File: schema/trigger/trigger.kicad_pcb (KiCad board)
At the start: 2 copper layers, 12 parts, among them J1 Barrel_Jack, Q1 DMG4800LK3-13

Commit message: some new packages
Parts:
- removed C5: 10mF/25V, Capacitor_THT:CP_Radial_D18.0mm_P7.50mm
- added C7: 10n, Capacitor_SMD:C_0603_1608Metric, F.Cu at (187.1, 19.3)
- added C8: 100n, Capacitor_SMD:C_0603_1608Metric, F.Cu at (187.1, 21.8)
- added D2: LED_Small, LED_SMD:LED_0805_2012Metric, F.Cu at (160.9, 49.1)
- added IC2: SSD1306, myLibrary:OLED_I2C_128x64_THT, F.Cu at (171.9, 21.1)
- added R10: 1k0, Resistor_SMD:R_0603_1608Metric, F.Cu at (187.1, 39.4)
- added R4: 860k, Resistor_SMD:R_0603_1608Metric, F.Cu at (187.1, 24.3)
- added R5: 100k, Resistor_SMD:R_0603_1608Metric, F.Cu at (187.1, 26.8)
- added R6: 1k0, Resistor_SMD:R_0603_1608Metric, F.Cu at (187.1, 29.3)
- added R7: 4k7, Resistor_SMD:R_0603_1608Metric, F.Cu at (187.1, 31.8)
- added R8: 4k7, Resistor_SMD:R_0603_1608Metric, F.Cu at (187.1, 34.4)
- added R9: 1k0, Resistor_SMD:R_0603_1608Metric, F.Cu at (187.1, 36.9)
- C1, C2, C3, C4: footprint Capacitor_THT:CP_Radial_D18.0mm_P7.50mm -> myLibrary:C_36x18; moved to B.Cu
- D1: value SS28 -> LED_Small; footprint Diode_SMD:D_SMB -> LED_SMD:LED_0805_2012Metric
- moved C1 90.6 mm to (71.1, 128.3), turned to 180 degrees
- moved C2 65.6 mm to (91.4, 128.3), turned to 180 degrees
- moved C3 44.5 mm to (111.8, 128.3), turned to 180 degrees
- moved C4 35.3 mm to (132.1, 128.3), turned to 180 degrees
- moved D1 34.8 mm to (160.9, 46.1)
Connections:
- D1 pad 1: VCC -> GND
- J1 pad 1: Net-(D1-A) -> VCC

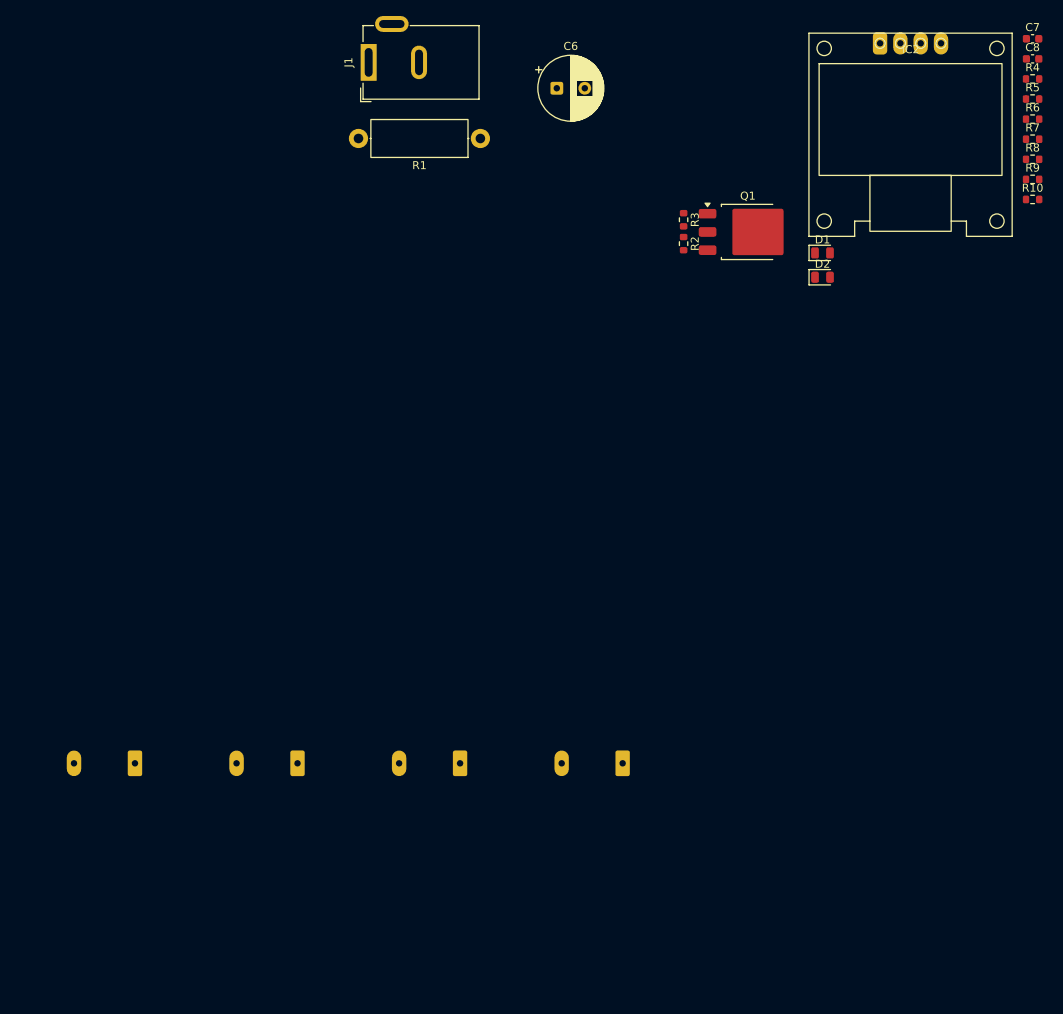
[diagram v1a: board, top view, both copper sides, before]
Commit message: yet another oled footprint
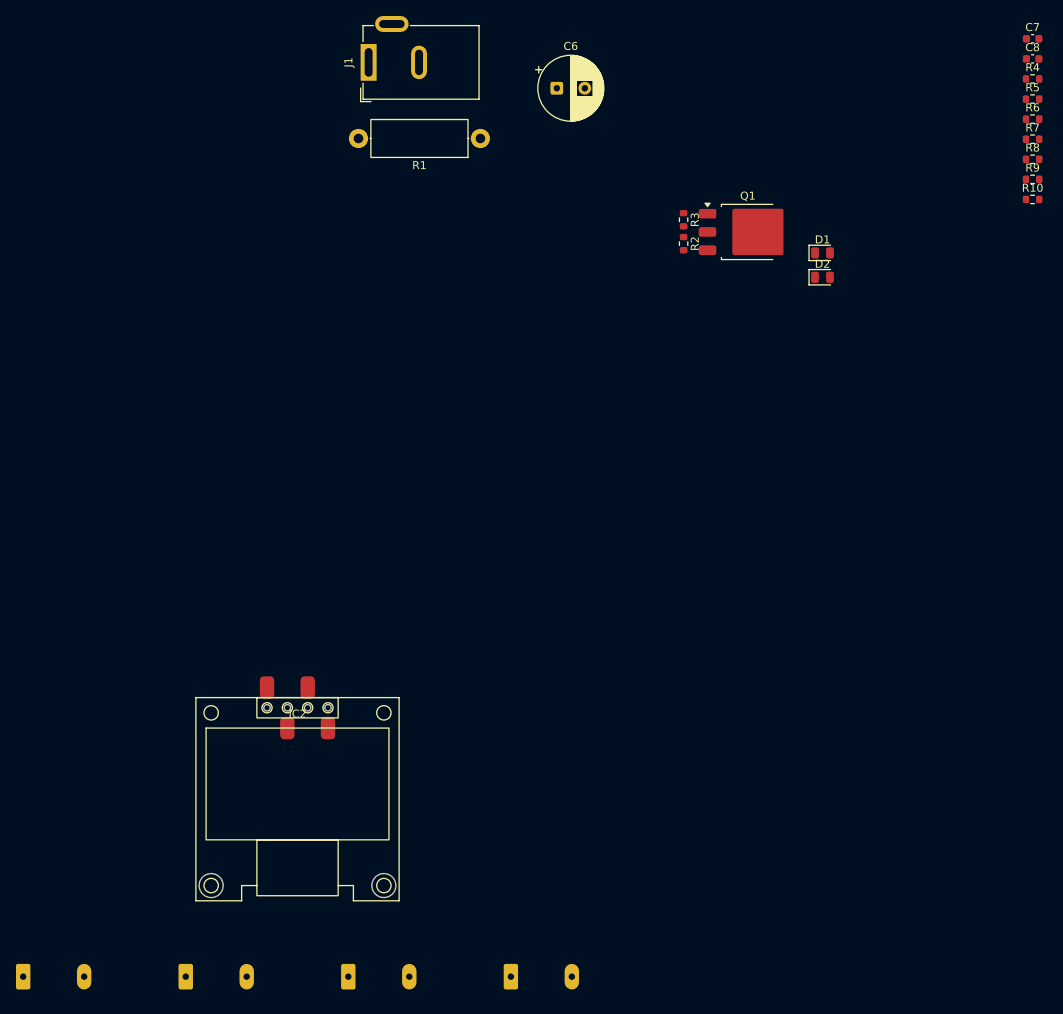
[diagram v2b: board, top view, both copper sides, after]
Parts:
- IC2: footprint myLibrary:OLED_I2C_128x64_THT -> myLibrary:OLED_I2C_128x64_SMD
- moved IC2 113.0 mm to (95.2, 104.2)
- moved C4 68.1 mm to (64.8, 118.1), turned to 0 degrees
- moved C1 55.5 mm to (125.7, 118.1), turned to 0 degrees
- moved C3 28.5 mm to (85.1, 118.1), turned to 0 degrees
- moved C2 17.3 mm to (105.4, 118.1), turned to 0 degrees

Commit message: pcb design
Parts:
- added C10: 100n, Capacitor_SMD:C_0603_1608Metric, F.Cu at (127.0, 117.5)
- added C11: 4u7, Capacitor_SMD:C_1206_3216Metric, F.Cu at (93.3, 101.6)
- added C12: 100n, Capacitor_SMD:C_0603_1608Metric, F.Cu at (69.8, 106.0)
- added C5: 100n, Capacitor_SMD:C_0603_1608Metric, F.Cu at (69.8, 102.9)
- added C9: 100n, Capacitor_SMD:C_0603_1608Metric, F.Cu at (92.7, 104.8)
- added D3: D_Schottky, Diode_SMD:D_SOD-123F, F.Cu at (92.1, 108.0)
- added IC1: RP2040_ZERO, myLibrary:RP2040_ZERO, F.Cu at (105.4, 111.8)
- added J2: Conn_01x05_Pin, myLibrary:Solder_Terminal_5p, F.Cu at (128.9, 121.3)
- added J4: Conn_01x04_Pin, myLibrary:Solder_Terminal_4p, F.Cu at (128.9, 104.8)
- added R11: 100R, Resistor_SMD:R_0603_1608Metric, F.Cu at (118.1, 100.3)
- added R12: 100R, Resistor_SMD:R_0603_1608Metric, F.Cu at (118.1, 102.9)
- added R13: 100R, Resistor_SMD:R_0603_1608Metric, F.Cu at (118.1, 115.6)
- added R14: 100R, Resistor_SMD:R_0603_1608Metric, F.Cu at (118.1, 113.0)
- added R15: 100R, Resistor_SMD:R_0603_1608Metric, F.Cu at (118.1, 111.1)
- added R16: 10k, Resistor_SMD:R_0603_1608Metric, F.Cu at (121.3, 113.0)
- added R17: 10k, Resistor_SMD:R_0603_1608Metric, F.Cu at (121.3, 111.1)
- added SW1: SW_Push, Button_Switch_SMD:SW_SPST_SKQG_WithStem, F.Cu at (105.5, 127.7)
- C4: value 10mF/25V -> 100n; footprint myLibrary:C_36x18 -> Capacitor_SMD:C_0603_1608Metric; moved to F.Cu
- C6, R1: moved to B.Cu
- IC2: value SSD1306 -> ~; footprint myLibrary:OLED_I2C_128x64_SMD -> myLibrary:Untitled_3
- J1: value Barrel_Jack -> Conn_01x06_Socket; footprint Connector_BarrelJack:BarrelJack_GCT_DCJ200-10-A_Horizontal -> myLibrary:Solder_Terminal_6p
- moved C7 141.1 mm to (96.5, 127.4), turned to -90 degrees
- moved R4 139.0 mm to (94.0, 127.4), turned to 90 degrees
- moved C8 135.0 mm to (87.6, 113.0), turned to 90 degrees
- moved R5 134.1 mm to (98.4, 127.4), turned to -90 degrees
- moved R10 133.1 mm to (88.1, 128.3)
- moved R9 133.1 mm to (88.1, 125.7)
- moved R6 132.0 mm to (85.1, 113.0), turned to 90 degrees
- moved R7 126.5 mm to (90.2, 113.0), turned to -90 degrees
- moved C6 121.0 mm to (72.8, 133.3), turned to 180 degrees
- moved R8 120.3 mm to (111.1, 127.6), turned to -90 degrees
- moved D1 110.5 mm to (84.3, 125.7)
- moved D2 110.2 mm to (84.3, 128.3)
- moved R1 106.0 mm to (73.0, 127.6), turned to 90 degrees
- moved Q1 103.0 mm to (82.1, 119.6), turned to 180 degrees
- moved J1 101.7 mm to (68.6, 117.5)
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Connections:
- C1 pad 1: Net-(J2-Pin_1) -> Net-(J1-Pin_3)
- C2 pad 1: Net-(J2-Pin_1) -> Net-(J1-Pin_3)
- C3 pad 1: Net-(J2-Pin_1) -> Net-(J1-Pin_3)
- C4 pad 1: Net-(J2-Pin_1) -> +5V
- IC2 pad 1: GND -> VCC
- IC2 pad 2: +3V3 -> GND
- IC2 pad 3: DISP_SCL -> Net-(D3-A)
- J1 pad 3: (no net) -> Net-(J1-Pin_3)
- Q1 pad 2: Net-(J2-Pin_2) -> Net-(J1-Pin_4)
- R1 pad 2: Net-(J2-Pin_1) -> Net-(J1-Pin_3)
- R4 pad 1: Net-(J2-Pin_1) -> Net-(J1-Pin_3)
- R6 pad 2: Net-(J3-Pin_1) -> Net-(J1-Pin_5)
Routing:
- net +5V: track 0.00 -> 89.1 mm, vias 0 -> 6
- net Net-(J1-Pin_3): track 0.00 -> 83.5 mm
- net +3V3: track 0.00 -> 76.7 mm, vias 0 -> 2
- net VCC: track 0.00 -> 44.9 mm, vias 0 -> 2
- net GND: track 0.00 -> 34.8 mm, vias 0 -> 47
- net Net-(D3-A): track 0.00 -> 24.3 mm, vias 0 -> 2
- net Net-(J1-Pin_4): track 0.00 -> 19.5 mm, vias 0 -> 3
- net Net-(J2-Pin_4): track 0.00 -> 19.3 mm
- net VSENSE: track 0.00 -> 18.1 mm, vias 0 -> 1
- net Net-(J1-Pin_5): track 0.00 -> 17.9 mm, vias 0 -> 1
- net LED: track 0.00 -> 16.3 mm
- net Net-(J2-Pin_5): track 0.00 -> 15.2 mm
- net LOCKED: track 0.00 -> 14.7 mm
- net BUTTON: track 0.00 -> 14.6 mm
- net Net-(J2-Pin_3): track 0.00 -> 14.1 mm
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- added copper zone on B.Cu, net GND
- added copper zone on F.Cu, net GND
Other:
- board outline added: 65.4 x 40.6 mm
- board text added: "+"
- board text added: "3V3 GND SCL SDA PIR"
- board text added: "5V0 GND TXD RXD"
- board text added: "GND"
- board text added: "LCK TR- TR+ GND +V"
- board text added: "OH2603"
- board text added: "https://github.com/ondrejh/kwokhaus"
- board text added: "v1.0"

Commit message: bom and some finetuning while first assembly
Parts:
- D1: value LED_Small -> LED_RED
- D2: value LED_Small -> LED_GREEN
- IC2: value ~ -> 5V0 step down
- R4: value 860k -> 1M0
